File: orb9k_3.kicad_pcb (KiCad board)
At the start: 2 copper layers, 49.3 x 33 mm, 23 parts, among them IC2 MAX3232, J1 DB9-PowerDTRRTS, J2 WM17143CT-ND, P1 USBV+D-, P2 USBD+GND, SW1 B3U-1000P, U1 ATSAMD21E18A_AU, U2 SPX3819M5, U3 6-pin-atmel-ice, U4 TC1240A

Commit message: modified footprint to remove solder pads around USB connector
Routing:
- net VBUS: track 41.2 -> 31.3 mm, vias 1 -> 0
- net D-: track 18.2 -> 25.4 mm, vias 0 -> 1
- net GND: track 107.7 -> 110.5 mm
- net Net-(IC2-Pad14): track 18.4 -> 16.0 mm
- net +3V3: track 68.6 -> 70.3 mm
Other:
- board text added: "Orb9k3 Test3"
- board text removed: "Orb9k3 Prod 1.0"

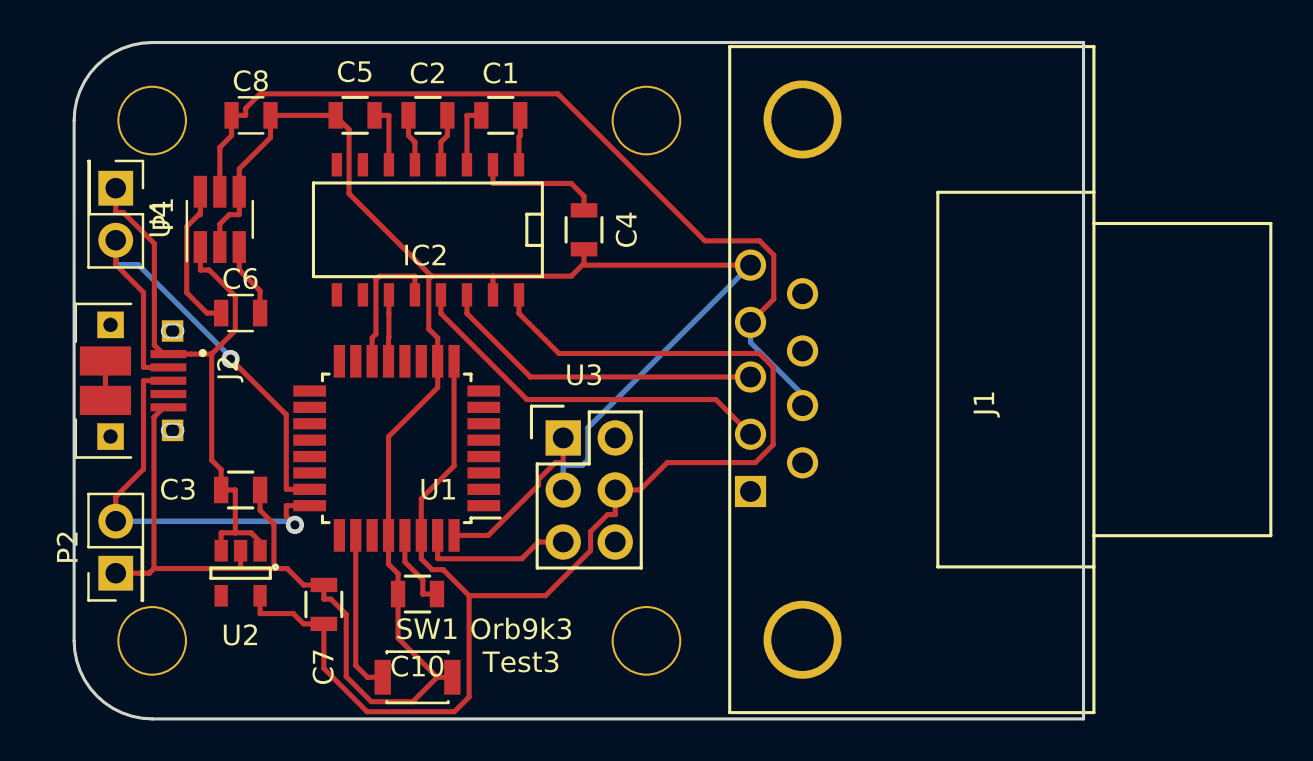
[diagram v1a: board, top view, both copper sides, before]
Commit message: changed schema and pcb to use xiao
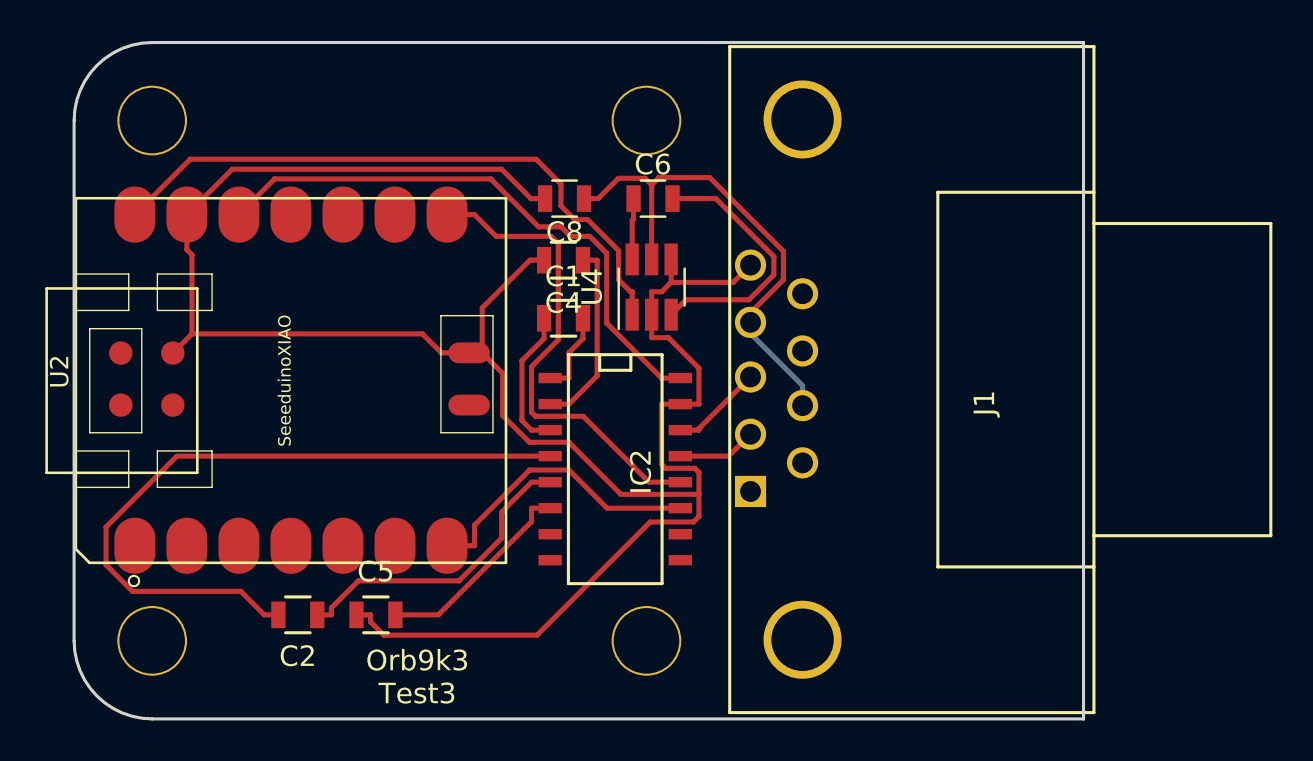
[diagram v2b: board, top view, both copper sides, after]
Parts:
- removed C10: 1uf, Resistors_SMD:R_0805
- removed C3: 10uf, Resistors_SMD:R_0805
- removed C7: 0.1uf, Resistors_SMD:R_0805
- removed J2: WM17143CT-ND, modules:FCI_10103594-0001LF
- removed P1: USBV+D-, Pin_Headers:Pin_Header_Straight_2x01_Pitch2.54mm
- removed P2: USBD+GND, Pin_Headers:Pin_Header_Straight_2x01_Pitch2.54mm
- removed SW1: B3U-1000P, modules:SW_B3U-1000P
- removed U1: ATSAMD21E18A_AU, Housings_QFP:TQFP-32_7x7mm_Pitch0.8mm
- removed U3: 6-pin-atmel-ice, Pin_Headers:Pin_Header_Straight_2x03
- U2: value SPX3819M5 -> SeeeduinoXIAO; footprint TO_SOT_Packages_SMD:SOT-23-5 -> modules:Seeeduino XIAO-MOUDLE14P-2.54-21X17.8MM
- moved C2 25.2 mm to (55.9, 103.9), turned to 0 degrees
- moved C5 24.4 mm to (59.7, 103.9)
- moved U4 21.3 mm to (73.2, 87.9)
- moved C6 20.9 mm to (73.3, 83.6)
- moved C8 15.8 mm to (68.9, 83.6), turned to 180 degrees
- moved IC2 14.8 mm to (71.4, 96.8), turned to 270 degrees
- moved U2 13.0 mm to (66.1, 101.4), turned to 90 degrees
- moved C1 10.4 mm to (68.9, 89.5)
- moved C4 1.79 mm to (68.9, 86.6), turned to 180 degrees
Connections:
- U2 pad 1: VBUS -> (no net)
- U2 pad 2: GND -> (no net)
- U2 pad 3: VBUS -> (no net)
- U2 pad 5: +3V3 -> (no net)
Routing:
- net +3V3: track 70.3 -> 28.3 mm
- net Net-(C2-Pad1): track 2.54 -> 34.4 mm
- net D-: track 25.4 -> 0.00 mm, vias 1 -> 0
- net D+: track 19.7 -> 0.00 mm, vias 1 -> 0
- net +10V: track 43.2 -> 24.8 mm
- net RX0: track 6.95 -> 23.5 mm
- net Net-(IC2-Pad13): track 18.5 -> 3.87 mm
- net Net-(C2-Pad2): track 2.54 -> 15.0 mm
- net Net-(IC2-Pad14): track 16.0 -> 4.55 mm
- net TX0: track 3.25 -> 14.3 mm
- net Net-(C6-Pad2): track 3.64 -> 12.8 mm
- net SWDIO: track 8.16 -> 0.00 mm
- net Net-(SW1-Pad1): track 7.90 -> 0.00 mm
- net SWCLK: track 7.61 -> 0.00 mm
- net Net-(C5-Pad2): track 3.11 -> 10.1 mm
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
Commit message: Updates to orb9k_3
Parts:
- renumbered C1 to .1, C2 to .1, C4 to .1, C5 to .1, C8 to 10, C6 to 10, U4 to ENSD, IC2 to STM3232
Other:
- board text added: "10"
- board text added: "Orb9k v3.0 www.thingotron.com"
- board text removed: "Orb9k3 Test3"
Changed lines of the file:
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@@
   (general
     (thickness 1.6)
-    (drawings 8)
+    (drawings 10)
     (tracks 146)
     (zones 0)
@@
     (0 F.Cu signal)
     (31 B.Cu signal)
-    (32 B.Adhes user)
-    (33 F.Adhes user)
+    (32 B.Adhes user hide)
+    (33 F.Adhes user hide)
     (34 B.Paste user)
     (35 F.Paste user)
@@
     (47 F.CrtYd user)
     (48 B.Fab user)
-    (49 F.Fab user)
+    (49 F.Fab user hide)
   )
   (setup
@@
     (visible_elements 7FFFFFFF)
     (pcbplotparams
-      (layerselection 0x010f8_80000001)
+      (layerselection 0x010f8_ffffffff)
       (usegerberextensions true)
       (usegerberattributes false)
@@
       (drillshape 0)
       (scaleselection 1)
-      (outputdirectory "../proto_orders/20170102/"))
+      (outputdirectory "../proto_orders/20200509/gerbers"))
   )
   (net 0 "")
@@
     (tags "resistor 0805")
     (attr smd)
-    (fp_text reference C1 (at 0 2.032 180) (layer F.SilkS)
-      (effects (font (size 1 1) (thickness 0.15)))
+    (fp_text reference .1 (at 0.016 2.794 180) (layer F.SilkS)
+      (effects (font (size 0.762 0.762) (thickness 0.1524)))
     )
     (fp_text value 0.1uf (at 0 2.1 180) (layer F.Fab)
@@
     (tags "resistor 0805")
     (attr smd)
-    (fp_text reference C2 (at 0 2.032 180) (layer F.SilkS)
-      (effects (font (size 1 1) (thickness 0.15)))
+    (fp_text reference .1 (at 0 0 180) (layer F.SilkS)
+      (effects (font (size 0.762 0.762) (thickness 0.1524)))
     )
     (fp_text value 0.1uf (at 0 2.1 180) (layer F.Fab)
@@
     (tags "resistor 0805")
     (attr smd)
-    (fp_text reference C4 (at 0 -2.1 180) (layer F.SilkS)
-      (effects (font (size 1 1) (thickness 0.15)))
+    (fp_text reference .1 (at 0.016 -2.8365 180) (layer F.SilkS)
+      (effects (font (size 0.762 0.762) (thickness 0.1524)))
     )
     (fp_text value 0.1uf (at 0 2.1 180) (layer F.Fab)
@@
     (tags "resistor 0805")
     (attr smd)
-    (fp_text reference C5 (at 0 -2.1) (layer F.SilkS)
-      (effects (font (size 1 1) (thickness 0.15)))
+    (fp_text reference .1 (at 0 0) (layer F.SilkS)
+      (effects (font (size 0.762 0.762) (thickness 0.1524)))
     )
     (fp_text value 0.1uf (at -0.508 -2.032) (layer F.Fab)
@@
     (tags "CMS SOJ")
     (attr smd)
-    (fp_text reference IC2 (at 0.127 -1.27 270) (layer F.SilkS)
+    (fp_text reference STM3232 (at 0 0 270 unlocked) (layer F.SilkS)
       (effects (font (size 1 1) (thickness 0.15)))
     )
@@
     (tags "resistor 0805")
     (attr smd)
-    (fp_text reference C8 (at 0 -1.65) (layer F.SilkS)
-      (effects (font (size 1 1) (thickness 0.15)))
+    (fp_text reference 10 (at 0.066 1.524) (layer F.SilkS)
+      (effects (font (size 0.762 0.762) (thickness 0.1524)))
     )
     (fp_text value 10uf (at 0 1.75) (layer F.Fab)
@@
     (tags "SOT-23-6 Handsoldering")
     (attr smd)
-    (fp_text reference U4 (at 0 -2.9 90) (layer F.SilkS)
-      (effects (font (size 1 1) (thickness 0.15)))
+    (fp_text reference ENSD (at 0 0 180) (layer F.SilkS)
+      (effects (font (size 0.762 0.762) (thickness 0.1524)))
     )
     (fp_text value TC1240A (at 0 2.9 90) (layer F.Fab)
@@
     (tags "resistor 0805")
     (attr smd)
-    (fp_text reference C6 (at 0 -1.65) (layer F.SilkS)
-      (effects (font (size 1 1) (thickness 0.15)))
+    (fp_text reference 10 (at 0.95 -1.524) (layer F.SilkS)
+      (effects (font (size 0.762 0.762) (thickness 0.15)))
     )
     (fp_text value 10uf (at 0 1.75) (layer F.Fab)
@@
     )
   )
-  (gr_text "Orb9k3\nTest3" (at 61.764 106.988) (layer F.SilkS)
+  (gr_text 10 (at 72.94 84.128) (layer F.Cu)
+    (effects (font (size 0.762 0.762) (thickness 0.1905)))
+  )
+  (gr_text 10 (at 72.94 83.62) (layer F.Cu)
+    (effects (font (size 0.762 0.762) (thickness 0.1905)))
+  )
+  (gr_text "Orb9k v3.0\nwww.thingotron.com" (at 62.78 106.988) (layer F.SilkS)
     (effects (font (size 1 1) (thickness 0.2)))
   )

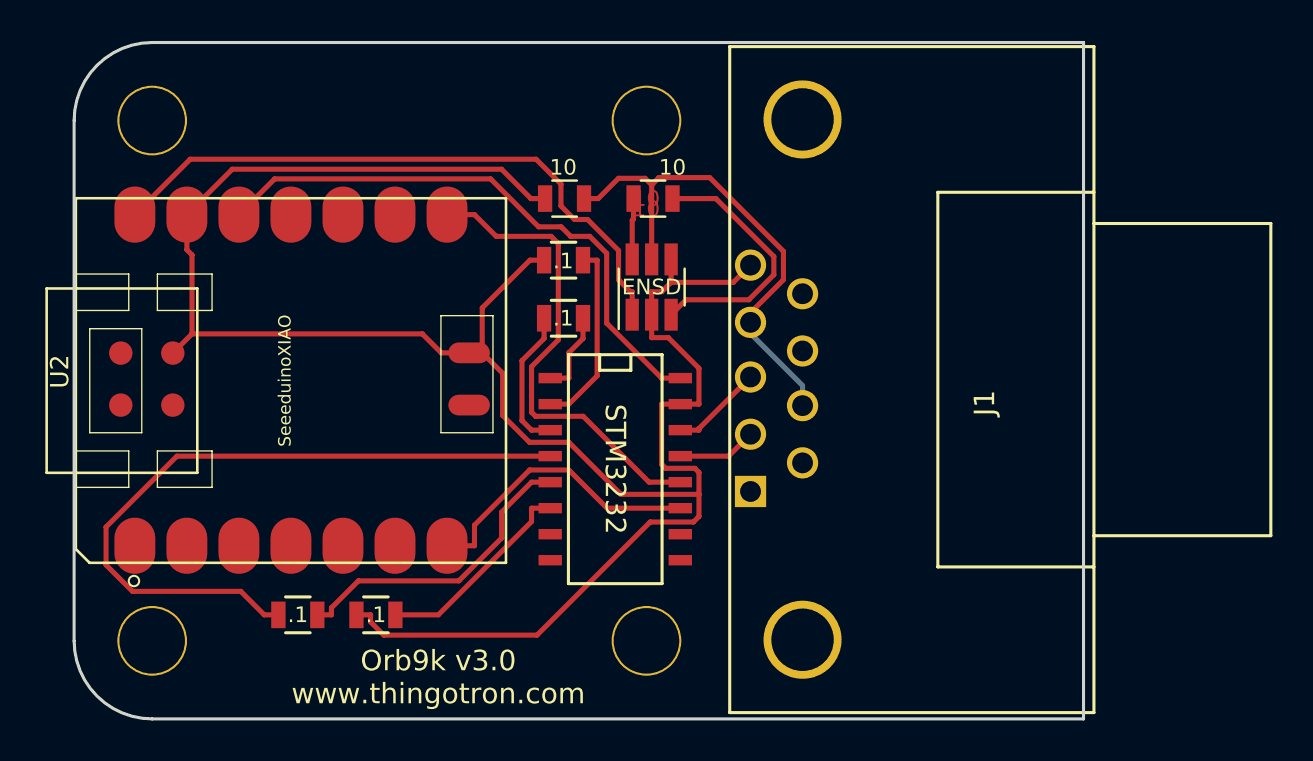
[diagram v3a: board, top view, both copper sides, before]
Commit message: added mark's 3d-printed case
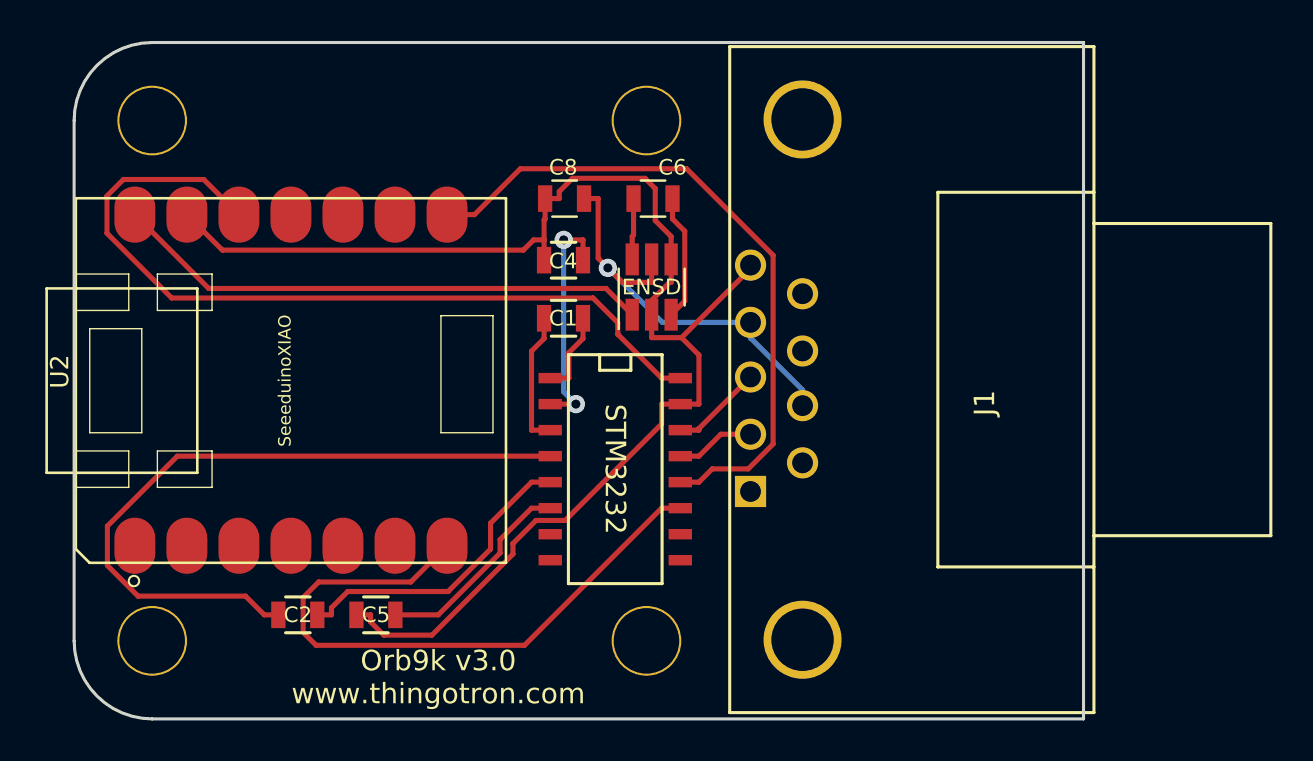
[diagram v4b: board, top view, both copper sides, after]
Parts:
- renumbered .1 to C1, .1 to C2, .1 to C4, .1 to C5, 10 to C6, 10 to C8
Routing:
- net GND: track 103.7 -> 68.5 mm
- net TX0: track 14.3 -> 31.2 mm
- net +3V3: track 28.3 -> 40.6 mm
- net RX0: track 23.5 -> 33.1 mm
- net Net-(C6-Pad2): track 12.8 -> 6.19 mm
- net VBUS: track 30.7 -> 26.3 mm
- net +10V: track 24.8 -> 21.0 mm, vias 0 -> 1
- net Net-(C4-Pad1): track 9.20 -> 11.4 mm, vias 0 -> 2
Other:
- board text removed: "10"
